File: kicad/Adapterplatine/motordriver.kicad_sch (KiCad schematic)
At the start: 11 parts, among them X10 Conn_01x04_Pin, X5 Conn_01x04_Pin, X6 Conn_01x04_Pin, X7 Conn_01x04_Pin, X9 Conn_01x04_Pin

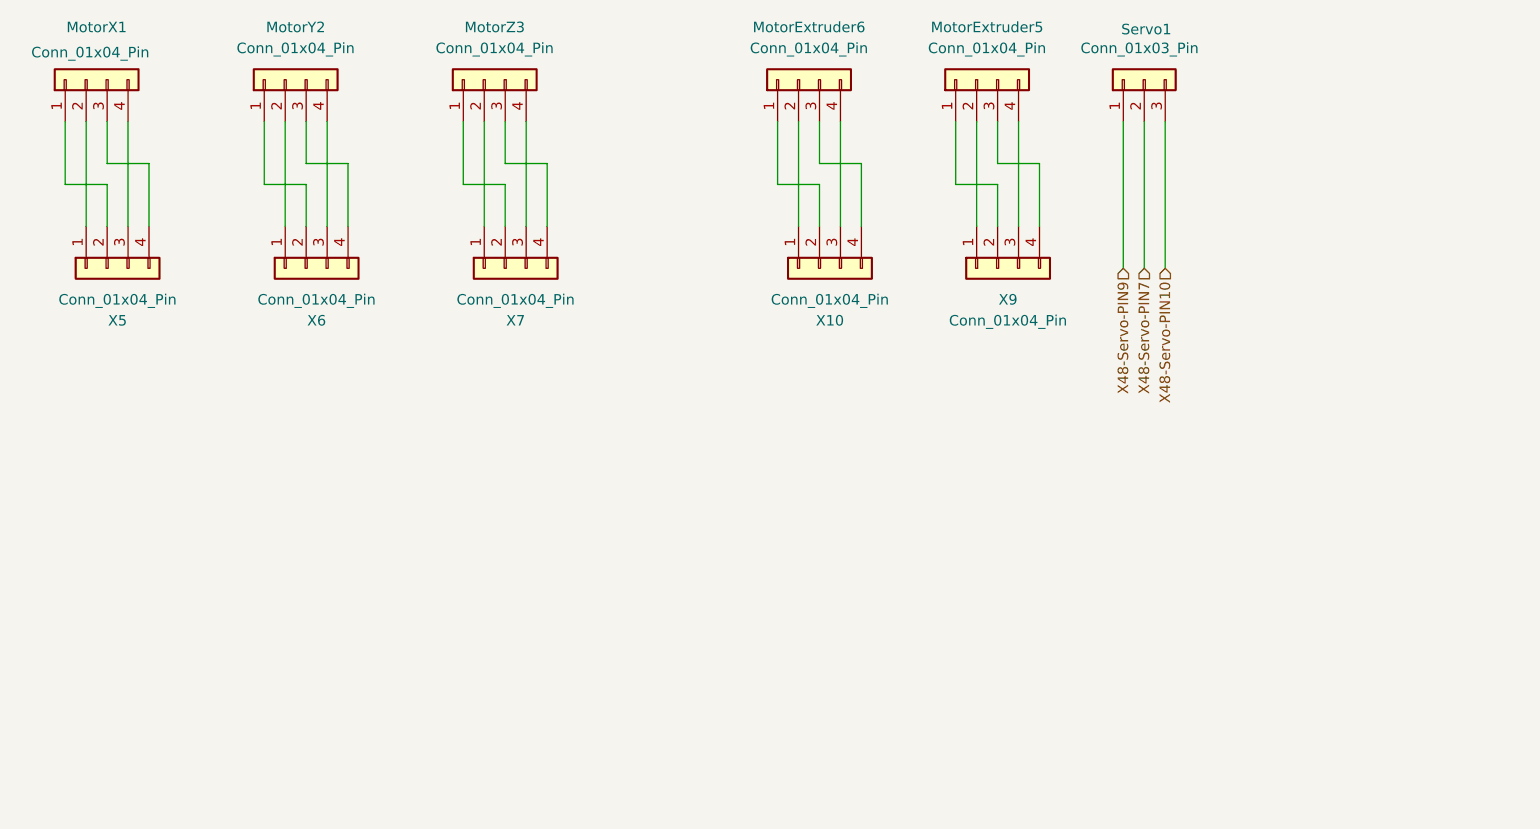
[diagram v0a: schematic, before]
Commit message: Abschlussbericht angefangen/ Adapterplatine ECR DCR
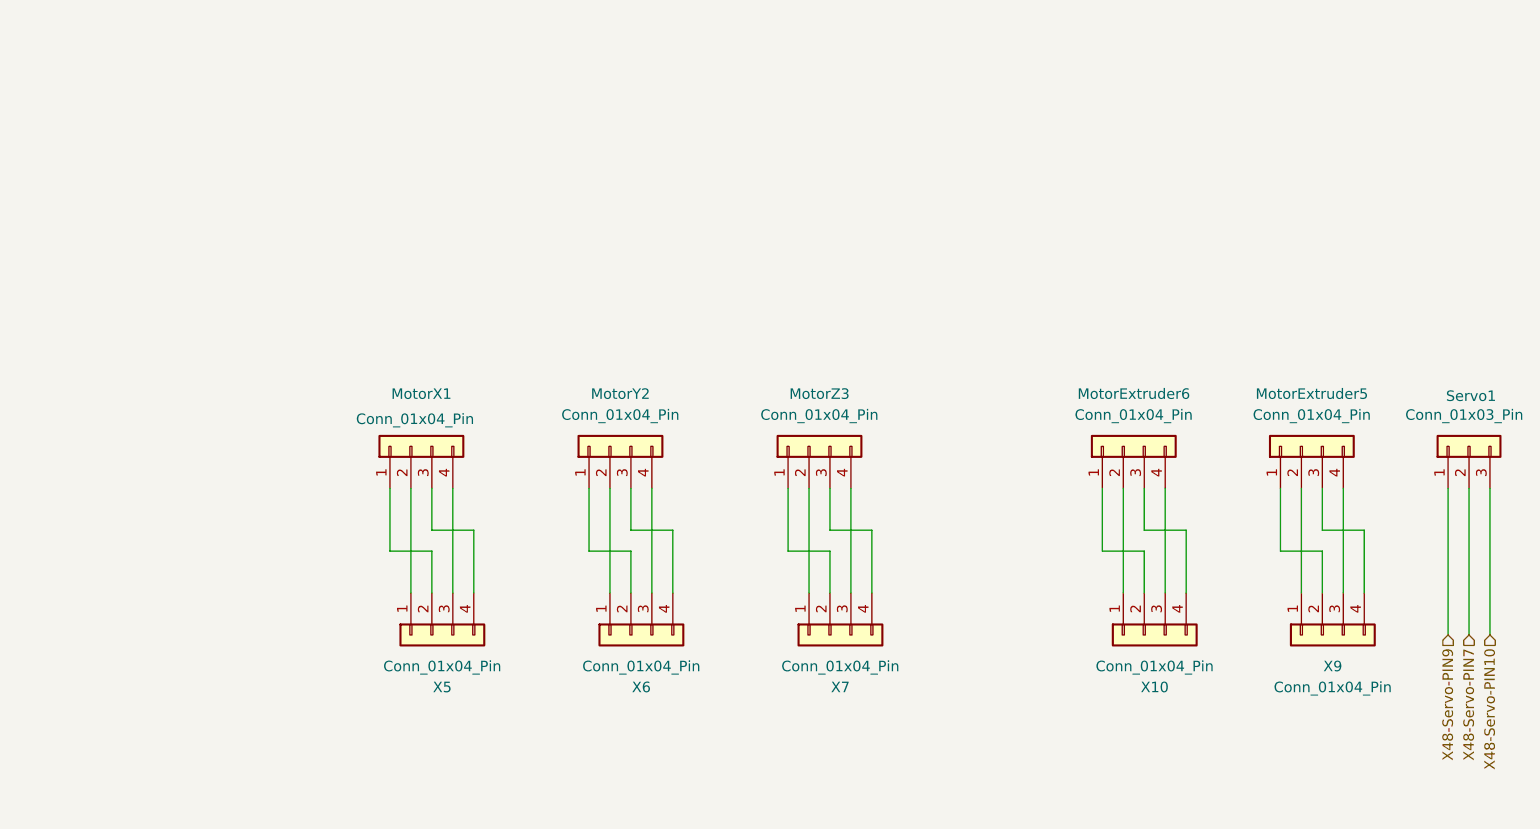
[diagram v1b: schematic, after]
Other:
- moved on the sheet: MotorExtruder5, MotorExtruder6, MotorX1, MotorY2, MotorZ3, Servo1, X10, X5, X6, X7, X9
